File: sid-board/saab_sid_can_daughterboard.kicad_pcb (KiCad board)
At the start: 2 copper layers, 50 x 50 mm, 15 parts, among them J1 Conn_02x10_Counter_Clockwise, Q1 BSS138, Q2 BSS138, Q3 BSS138, Q4 BSS138, U3 PCA82C250, U4 PCA82C250

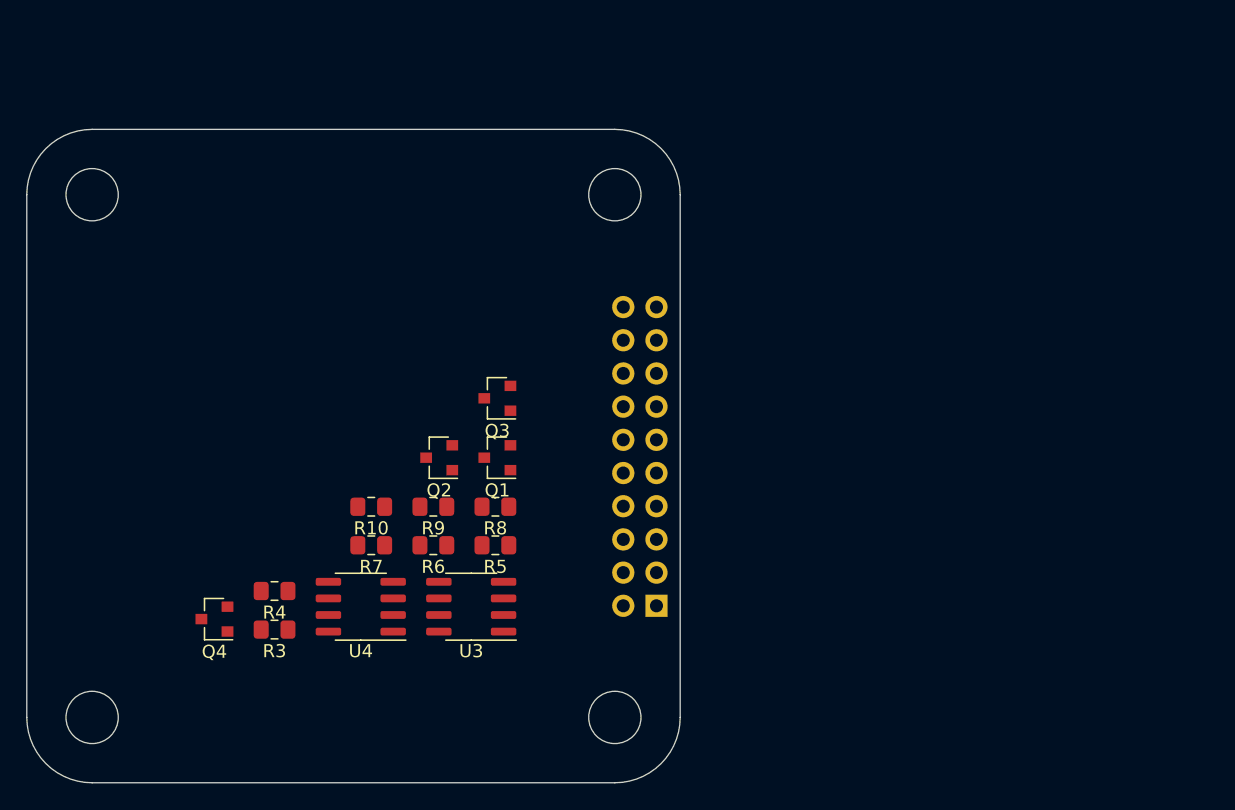
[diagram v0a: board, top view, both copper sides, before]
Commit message: Working on CAN daughterboard
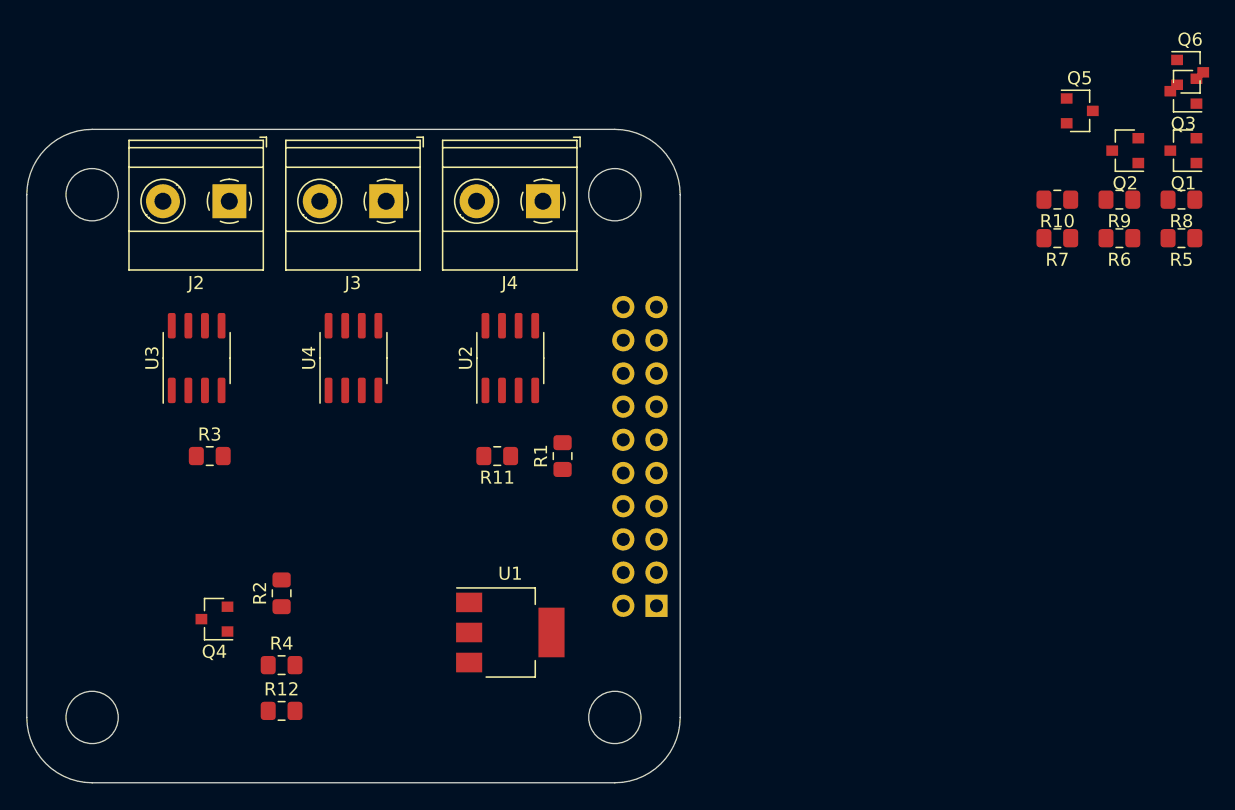
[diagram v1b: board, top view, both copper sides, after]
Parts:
- added J2: Screw_Terminal_01x02, TerminalBlock_Phoenix:TerminalBlock_Phoenix_MKDS-1,5-2-5.08_1x02_P5.08mm_Horizontal, F.Cu at (185.5, 77.5)
- added J3: Screw_Terminal_01x02, TerminalBlock_Phoenix:TerminalBlock_Phoenix_MKDS-1,5-2-5.08_1x02_P5.08mm_Horizontal, F.Cu at (197.5, 77.5)
- added J4: Screw_Terminal_01x02, TerminalBlock_Phoenix:TerminalBlock_Phoenix_MKDS-1,5-2-5.08_1x02_P5.08mm_Horizontal, F.Cu at (209.5, 77.5)
- added Q5: BSS138, Package_TO_SOT_SMD:SOT-23, F.Cu at (250.6, 70.6)
- added Q6: BSS138, Package_TO_SOT_SMD:SOT-23, F.Cu at (259.0, 67.6)
- added R1: 10k, Resistor_SMD:R_0805_2012Metric_Pad1.15x1.40mm_HandSolder, F.Cu at (211.0, 97.0)
- added R11: 10k, Resistor_SMD:R_0805_2012Metric_Pad1.15x1.40mm_HandSolder, F.Cu at (206.0, 97.0)
- added R12: 10k, Resistor_SMD:R_0805_2012Metric_Pad1.15x1.40mm_HandSolder, F.Cu at (189.5, 116.5)
- added R2: 10k, Resistor_SMD:R_0805_2012Metric_Pad1.15x1.40mm_HandSolder, F.Cu at (189.5, 107.5)
- added U1: NCP1117-5.0_SOT223, Package_TO_SOT_SMD:SOT-223-3_TabPin2, F.Cu at (207.0, 110.5)
- added U2: PCA82C250, Package_SO:SOIC-8_3.9x4.9mm_P1.27mm, F.Cu at (207.0, 89.5)
- moved Q1 57.5 mm to (258.5, 73.6)
- moved Q3 57.5 mm to (258.5, 69.1)
- moved Q2 57.5 mm to (254.1, 73.6)
- moved R10 57.5 mm to (248.9, 77.4)
- moved R6 57.5 mm to (253.6, 80.3)
- moved R7 57.5 mm to (248.9, 80.3)
- moved R9 57.5 mm to (253.6, 77.4)
- moved R5 57.5 mm to (258.4, 80.3)
- moved R8 57.5 mm to (258.4, 77.4)
- moved U3 28.3 mm to (183.0, 89.5), turned to 90 degrees
- moved U4 19.0 mm to (195.0, 89.5), turned to 90 degrees
- moved R3 14.2 mm to (184.0, 97.0), turned to 0 degrees
- moved R4 5.70 mm to (189.5, 113.0), turned to 0 degrees
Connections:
- J1 pad 1: Net-(J1-Pad1) -> V_IN
- J1 pad 10: Net-(J1-Pad10) -> RXA
- J1 pad 11: Net-(J1-Pad11) -> TXB
- J1 pad 12: Net-(J1-Pad12) -> RXB
- J1 pad 13: Net-(J1-Pad13) -> TXC
- J1 pad 14: Net-(J1-Pad14) -> RXC
- J1 pad 15: Net-(J1-Pad15) -> (no net)
- J1 pad 16: Net-(J1-Pad16) -> (no net)
- J1 pad 17: Net-(J1-Pad17) -> (no net)
- J1 pad 18: Net-(J1-Pad18) -> (no net)
- J1 pad 19: Net-(J1-Pad19) -> (no net)
- J1 pad 2: Net-(J1-Pad2) -> GND
- J1 pad 20: Net-(J1-Pad20) -> (no net)
- J1 pad 3: Net-(J1-Pad3) -> VDD_3.3V
- J1 pad 4: Net-(J1-Pad4) -> GND
- J1 pad 5: Net-(J1-Pad5) -> (no net)
- J1 pad 6: Net-(J1-Pad6) -> (no net)
- J1 pad 7: Net-(J1-Pad7) -> (no net)
- J1 pad 8: Net-(J1-Pad8) -> (no net)
- J1 pad 9: Net-(J1-Pad9) -> TXA
- U3 pad 5: Net-(U3-Pad5) -> (no net)
- U4 pad 5: Net-(U4-Pad5) -> (no net)
